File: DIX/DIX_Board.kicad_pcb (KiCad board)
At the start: 2 copper layers, 32 parts, among them J1 Conn_01x12_Male, J2 Conn_01x12_Male, U1 AMS1117-3.3, U3 TPS79318-EP

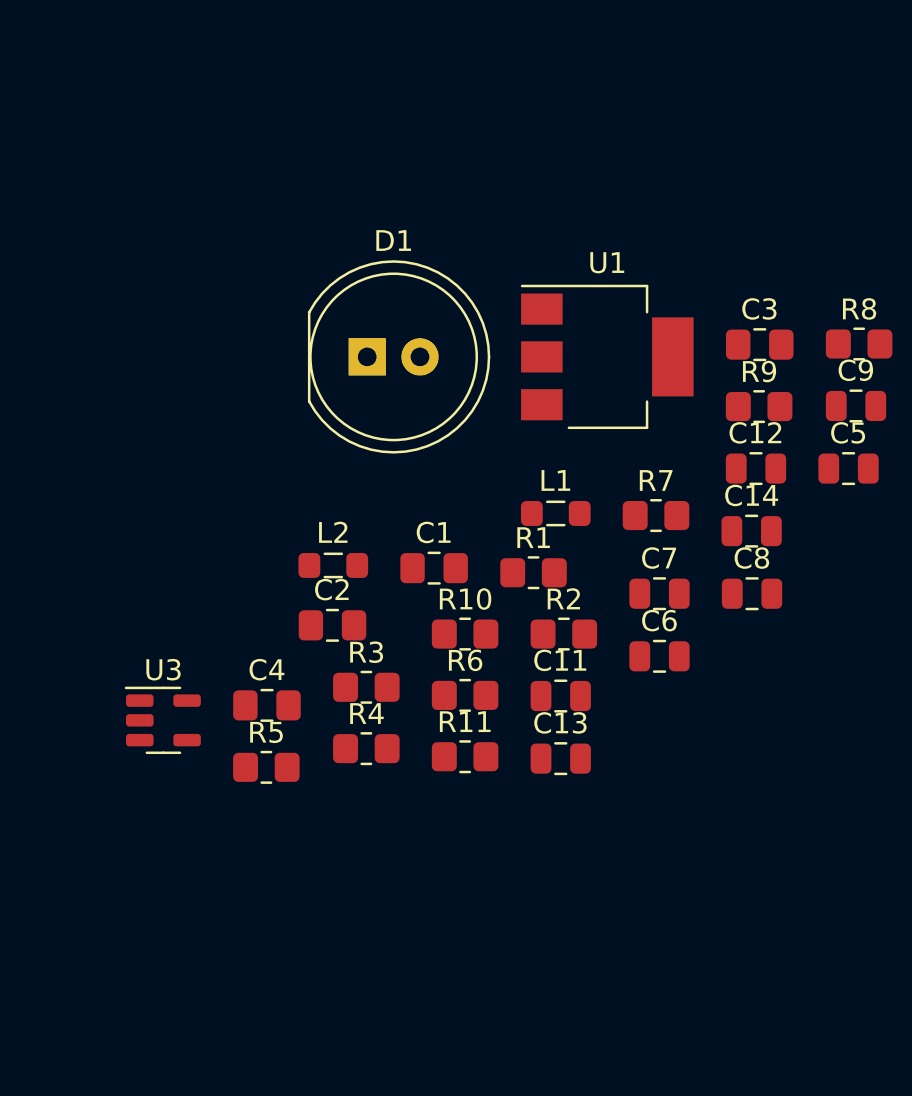
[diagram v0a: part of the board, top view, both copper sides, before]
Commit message: Less electrical check failures
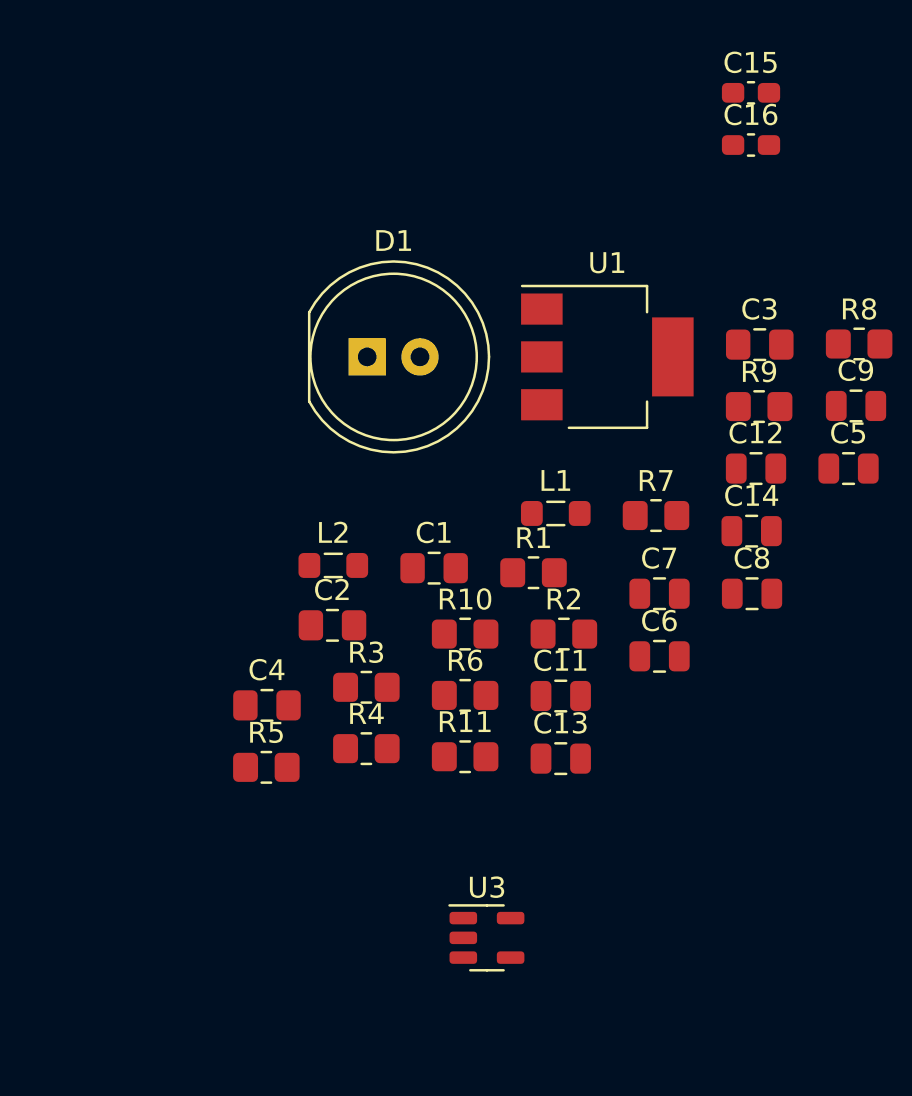
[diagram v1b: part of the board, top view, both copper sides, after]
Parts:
- added C15: 0.1uF, Capacitor_SMD:C_0603_1608Metric_Pad1.08x0.95mm_HandSolder, F.Cu at (149.9, 63.5)
- added C16: 0.1uF, Capacitor_SMD:C_0603_1608Metric_Pad1.08x0.95mm_HandSolder, F.Cu at (149.9, 66.0)
- moved U3 18.7 mm to (137.2, 104.1)
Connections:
- C12 pad 2: Net-(C12-Pad2) -> GND
- C13 pad 2: Net-(C12-Pad2) -> GND
- C14 pad 2: Net-(C12-Pad2) -> GND
- C3 pad 2: Net-(C3-Pad2) -> GND
- C4 pad 2: Net-(C4-Pad2) -> GND
- C5 pad 2: Net-(C5-Pad2) -> GND
- C7 pad 2: Net-(C5-Pad2) -> GND
- J2 pad 1: unconnected-(J2-Pad1) -> MCLK
- U3 pad 2: Net-(C12-Pad2) -> GND

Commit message: Some routing
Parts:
- added IC1: TORX1950A_F_, Audio_Module:Reverb_BTDR-1H, F.Cu at (48.6, 53.6)
- added IC2: TORX1950A_F_, Audio_Module:Reverb_BTDR-1H, F.Cu at (48.6, 96.8)
- added U2: DIX4192IPFB, DIX Footprints:DIX4192IPFB, F.Cu at (73.7, 144.8)
- moved U1 134.4 mm to (40.0, 162.6), turned to 180 degrees
- moved R8 116.0 mm to (58.4, 139.7)
- moved D1 115.8 mm to (38.1, 144.8)
- moved C1 115.6 mm to (48.1, 163.0), turned to -90 degrees
- moved C16 114.3 mm to (58.4, 134.6), turned to 180 degrees
- moved C15 111.3 mm to (60.1, 129.4)
- moved R9 99.5 mm to (58.4, 116.8)
- moved R11 98.6 mm to (50.8, 144.8), turned to 180 degrees
- moved C13 91.1 mm to (80.1, 163.5), turned to 90 degrees
- moved J2 90.2 mm to (106.1, 185.4), turned to -90 degrees
- moved R4 89.7 mm to (58.4, 147.3), turned to 180 degrees
- moved C12 89.6 mm to (111.8, 162.6), turned to 180 degrees
- moved C14 88.2 mm to (104.1, 160.0), turned to 180 degrees
- moved U3 88.0 mm to (73.7, 165.1), turned to -90 degrees
- moved C5 86.4 mm to (113.3, 157.5), turned to 180 degrees
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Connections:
- J1 pad 10: unconnected-(J1-Pad10) -> SDOUTB
- J1 pad 2: unconnected-(J1-Pad2) -> MCLK
- J1 pad 3: unconnected-(J1-Pad3) -> BCKA
- J1 pad 4: unconnected-(J1-Pad4) -> LRCKA
- J1 pad 5: unconnected-(J1-Pad5) -> SDINA
- J1 pad 6: unconnected-(J1-Pad6) -> SDOUTA
- J1 pad 7: unconnected-(J1-Pad7) -> BCKB
- J1 pad 8: unconnected-(J1-Pad8) -> LRCKB
- J1 pad 9: unconnected-(J1-Pad9) -> SDINB
- J2 pad 1: MCLK -> +5V
- J2 pad 10: unconnected-(J2-Pad10) -> CCLK/SCL
- J2 pad 11: unconnected-(J2-Pad11) -> *CS/AO
- J2 pad 12: unconnected-(J2-Pad12) -> CPM
- J2 pad 2: unconnected-(J2-Pad2) -> TX+
- J2 pad 3: unconnected-(J2-Pad3) -> TX-
- J2 pad 4: unconnected-(J2-Pad4) -> GPO4
- J2 pad 5: unconnected-(J2-Pad5) -> GPO3
- J2 pad 6: unconnected-(J2-Pad6) -> GPO2
- J2 pad 7: unconnected-(J2-Pad7) -> GPO1
- J2 pad 8: unconnected-(J2-Pad8) -> CDOUT/SDA
- J2 pad 9: unconnected-(J2-Pad9) -> CDIN/A1
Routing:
- net +3.3V: track 0.00 -> 127.9 mm
- net Net-(C4-Pad1): track 0.00 -> 81.3 mm
- net +5V: track 0.00 -> 68.5 mm
- net GND: track 0.00 -> 59.3 mm
- net Net-(R11-Pad1): track 0.00 -> 58.5 mm
- net VBUS: track 0.00 -> 56.7 mm
- net SDOUTA: track 0.00 -> 50.0 mm
- net Net-(R5-Pad1): track 0.00 -> 22.0 mm
- net Net-(C15-Pad2): track 0.00 -> 20.3 mm
- net Net-(C10-Pad2): track 0.00 -> 9.96 mm
- net +1V8: track 0.00 -> 7.84 mm
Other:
- board outline added: 121.9 x 177.8 mm
